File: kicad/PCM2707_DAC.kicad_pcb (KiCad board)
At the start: 2 copper layers, 49.5 x 38.1 mm, 37 parts, among them CON1 GND_CONNECTORSMD, J1 USB, Q1 12MHz, U1 PCM2707C

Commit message: Revert "Revert "Rounded corners on design, adding kicad generated gerbers""
This reverts commit e5d359f14d2e2aadcde64fe7d354a7193523fc92.
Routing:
- net /N$18: track 5.16 -> 3.01 mm
- net /N$17: track 5.04 -> 2.94 mm
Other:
- board size 49.5 x 38.1 mm -> 49.5 x 37.8 mm
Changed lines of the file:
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@@
     (links 79)
     (no_connects 0)
-    (area 148.704299 55.994299 198.259701 94.119701)
+    (area 147.0025 54.7497 198.20029 98.75012)
     (thickness 1.6)
     (drawings 6)
-    (tracks 211)
+    (tracks 209)
     (zones 0)
     (modules 37)
@@
     (40 Dwgs.User user)
     (41 Cmts.User user)
-    (42 Eco1.User user)
-    (43 Eco2.User user)
+    (42 Eco1.User user hide)
+    (43 Eco2.User user hide)
     (44 Edge.Cuts user)
   )
@@
     (pad_to_mask_clearance 0.2)
     (aux_axis_origin 0 0)
-    (visible_elements FFFFFFFF)
+    (visible_elements FFFDFFBF)
     (pcbplotparams
-      (layerselection 0x00030_80000001)
+      (layerselection 0x010ec_80000001)
       (usegerberextensions true)
       (excludeedgelayer true)
@@
       (outputformat 1)
       (mirror false)
-      (drillshape 1)
+      (drillshape 0)
       (scaleselection 1)
-      (outputdirectory ""))
+      (outputdirectory gerbers/))
   )
   (net 0 "")
@@
       (net 26 OL))
   )
-  (gr_line (start 198.247 56.007) (end 198.247 87.727) (layer Edge.Cuts) (width 0.0254))
-  (gr_line (start 198.247 87.727) (end 193.137 94.107) (layer Edge.Cuts) (width 0.0254))
-  (gr_line (start 193.137 94.107) (end 155.097 94.107) (layer Edge.Cuts) (width 0.0254))
-  (gr_line (start 155.097 94.107) (end 148.717 86.457) (layer Edge.Cuts) (width 0.0254))
-  (gr_line (start 148.717 86.457) (end 148.717 56.007) (layer Edge.Cuts) (width 0.0254))
-  (gr_line (start 148.717 56.007) (end 198.247 56.007) (layer Edge.Cuts) (width 0.0254))
+  (gr_line (start 198.12 56.134) (end 198.12 87.63) (angle 90) (layer Edge.Cuts) (width 0.15))
+  (gr_line (start 148.59 56.134) (end 198.12 56.134) (angle 90) (layer Edge.Cuts) (width 0.15))
+  (gr_line (start 148.59 86.868) (end 148.59 56.134) (angle 90) (layer Edge.Cuts) (width 0.15))
+  (gr_line (start 192.278 93.98) (end 155.702 93.98) (angle 90) (layer Edge.Cuts) (width 0.15))
+  (gr_arc (start 155.702 86.868) (end 155.702 93.98) (angle 90) (layer Edge.Cuts) (width 0.15))
+  (gr_arc (start 192.024 87.884) (end 198.12 87.63) (angle 90) (layer Edge.Cuts) (width 0.15))
   (segment (start 161.4424 70.555) (end 160.459 70.555) (width 0.4064) (layer Top) (net 1) (status 10))
   (segment (start 160.459 70.555) (end 159.119 69.215) (width 0.4064) (layer Top) (net 1) (status 20))
@@
   (segment (start 170.0276 72.955) (end 172.28 72.955) (width 0.4064) (layer Top) (net 8) (status 10))
   (segment (start 172.28 72.955) (end 172.72 73.395) (width 0.4064) (layer Top) (net 8) (status 20))
-  (segment (start 180.9115 70.11416) (end 178.1175 70.11416) (width 0.254) (layer Top) (net 9))
-  (segment (start 178.1175 70.11416) (end 178.06416 70.1675) (width 0.254) (layer Top) (net 9))
-  (segment (start 178.765 70.1675) (end 180.859 70.1675) (width 0.4064) (layer Top) (net 9) (status 30))
+  (segment (start 180.9115 70.11416) (end 178.1175 70.11416) (width 0.254) (layer Top) (net 9) (status 30))
+  (segment (start 178.1175 70.11416) (end 178.06416 70.1675) (width 0.254) (layer Top) (net 9) (status 30))
   (segment (start 180.859 70.1675) (end 180.9115 70.115) (width 0.4064) (layer Top) (net 9) (status 30))
-  (segment (start 178.06416 73.3425) (end 180.92166 73.3425) (width 0.254) (layer Top) (net 10))
-  (segment (start 180.92166 73.3425) (end 180.975 73.39584) (width 0.254) (layer Top) (net 10))
-  (segment (start 178.765 73.3425) (end 180.9225 73.3425) (width 0.4064) (layer Top) (net 10) (status 30))
+  (segment (start 178.06416 73.3425) (end 180.92166 73.3425) (width 0.254) (layer Top) (net 10) (status 30))
+  (segment (start 180.92166 73.3425) (end 180.975 73.39584) (width 0.254) (layer Top) (net 10) (status 30))
   (segment (start 180.9225 73.3425) (end 180.975 73.395) (width 0.4064) (layer Top) (net 10) (status 30))
   (segment (start 167.735 67.4624) (end 167.735 65.045) (width 0.4064) (layer Top) (net 11) (status 30))
   (segment (start 167.735 65.045) (end 168.01 64.77) (width 0.4064) (layer Top) (net 11) (status 30))
   (segment (start 170.0276 71.355) (end 174.3775 71.355) (width 0.4064) (layer Top) (net 12) (status 10))
-  (segment (start 174.3775 71.355) (end 175.565 70.1675) (width 0.4064) (layer Top) (net 12) (status 20))
-  (segment (start 175.565 70.1675) (end 176.2125 70.1675) (width 0.4064) (layer Top) (net 12) (status 10))
-  (segment (start 176.2125 70.1675) (end 177.8 68.58) (width 0.4064) (layer Top) (net 12))
+  (segment (start 174.3775 71.355) (end 175.565 70.1675) (width 0.4064) (layer Top) (net 12))
+  (segment (start 175.565 70.1675) (end 176.2125 70.1675) (width 0.4064) (layer Top) (net 12) (status 20))
+  (segment (start 176.2125 70.1675) (end 177.8 68.58) (width 0.4064) (layer Top) (net 12) (status 10))
   (segment (start 177.8 68.58) (end 179.07 68.58) (width 0.4064) (layer Top) (net 12))
   (segment (start 179.07 68.58) (end 179.705 67.945) (width 0.4064) (layer Top) (net 12))
@@
   (segment (start 157.365 69.215) (end 157.365 67.46) (width 0.4064) (layer Top) (net 13) (status 30))
   (segment (start 157.365 67.46) (end 157.215 67.31) (width 0.4064) (layer Top) (net 13) (status 30))
-  (segment (start 175.565 73.3425) (end 176.26584 73.3425) (width 0.254) (layer Top) (net 14))
+  (segment (start 175.565 73.3425) (end 176.26584 73.3425) (width 0.254) (layer Top) (net 14) (status 20))
   (segment (start 170.0276 72.155) (end 174.3775 72.155) (width 0.4064) (layer Top) (net 14) (status 10))
-  (segment (start 174.3775 72.155) (end 175.565 73.3425) (width 0.4064) (layer Top) (net 14) (status 20))
-  (segment (start 175.565 73.3425) (end 175.565 76.2) (width 0.4064) (layer Top) (net 14) (status 30))
+  (segment (start 174.3775 72.155) (end 175.565 73.3425) (width 0.4064) (layer Top) (net 14))
+  (segment (start 175.565 73.3425) (end 175.565 76.2) (width 0.4064) (layer Top) (net 14) (status 20))
   (segment (start 175.565 76.2) (end 175.565 78.194) (width 0.4064) (layer Top) (net 14) (status 30))
   (segment (start 175.565 78.194) (end 175.26 78.499) (width 0.4064) (layer Top) (net 14) (status 30))
@@
   (segment (start 167.005 81.165) (end 160.17 81.165) (width 0.4064) (layer Top) (net 23))
   (segment (start 160.17 81.165) (end 159.385 80.38) (width 0.4064) (layer Top) (net 23) (status 20))
-  (segment (start 168.91 90.805) (end 174.625 90.805) (width 0.254) (layer Bottom) (net 24))
+  (segment (start 168.91 90.805) (end 174.625 90.805) (width 0.254) (layer Bottom) (net 24) (status 10))
   (via (at 175.26 90.17) (size 0.889) (drill 0.635) (layers Top Bottom) (net 24))
-  (segment (start 175.26 90.17) (end 175.26 87.89416) (width 0.254) (layer Top) (net 24))
+  (segment (start 175.26 90.17) (end 175.26 87.89416) (width 0.254) (layer Top) (net 24) (status 20))
   (segment (start 174.625 90.805) (end 175.26 90.17) (width 0.254) (layer Bottom) (net 24))
   (via (at 172.72 76.835) (size 0.9048) (drill 0.6) (layers Top Bottom) (net 24))
@@
   (segment (start 189.495 60.0075) (end 189.495 58.155) (width 0.4064) (layer Top) (net 24) (status 10))
   (segment (start 189.495 58.155) (end 189.5475 58.1025) (width 0.4064) (layer Top) (net 24))
-  (segment (start 162.59 90.17) (end 162.59 88.87) (width 0.254) (layer Top) (net 25))
+  (segment (start 162.59 90.17) (end 162.59 88.87) (width 0.254) (layer Top) (net 25) (status 10))
   (via (at 163.83 87.63) (size 0.889) (drill 0.635) (layers Top Bottom) (net 25))
   (segment (start 162.59 88.87) (end 163.83 87.63) (width 0.254) (layer Top) (net 25))
-  (segment (start 167.005 90.805) (end 167.64 90.805) (width 0.254) (layer Bottom) (net 25))
+  (segment (start 167.005 90.805) (end 167.64 90.805) (width 0.254) (layer Bottom) (net 25) (status 30))
   (via (at 164.7825 78.105) (size 0.9048) (drill 0.6) (layers Top Bottom) (net 25))
   (via (at 166.0525 65.7225) (size 0.9048) (drill 0.6) (layers Top Bottom) (net 25))
@@
       (pts
         (xy 148.717 56.007) (xy 177.636494 55.980006) (xy 177.8 66.775006) (xy 172.72 66.675) (xy 167.64 70.485)
-        (xy 167.767 94.107) (xy 155.785991 94.107) (xy 148.717 88.392)
+        (xy 167.767 94.107) (xy 155.785991 94.107) (xy 151.384 92.456) (xy 148.717 88.392)
       )
     )
@@
     (polygon
       (pts
-        (xy 168.91 93.98) (xy 192.405 93.98) (xy 198.12 88.9) (xy 198.12 56.515) (xy 179.07 56.515)
-        (xy 179.07 67.945) (xy 173.355 67.945) (xy 168.91 71.12)
+        (xy 168.91 93.98) (xy 192.405 93.98) (xy 195.58 92.71) (xy 198.12 88.9) (xy 198.12 56.515)
+        (xy 179.07 56.515) (xy 179.07 67.945) (xy 173.355 67.945) (xy 168.91 71.12)
       )
     )

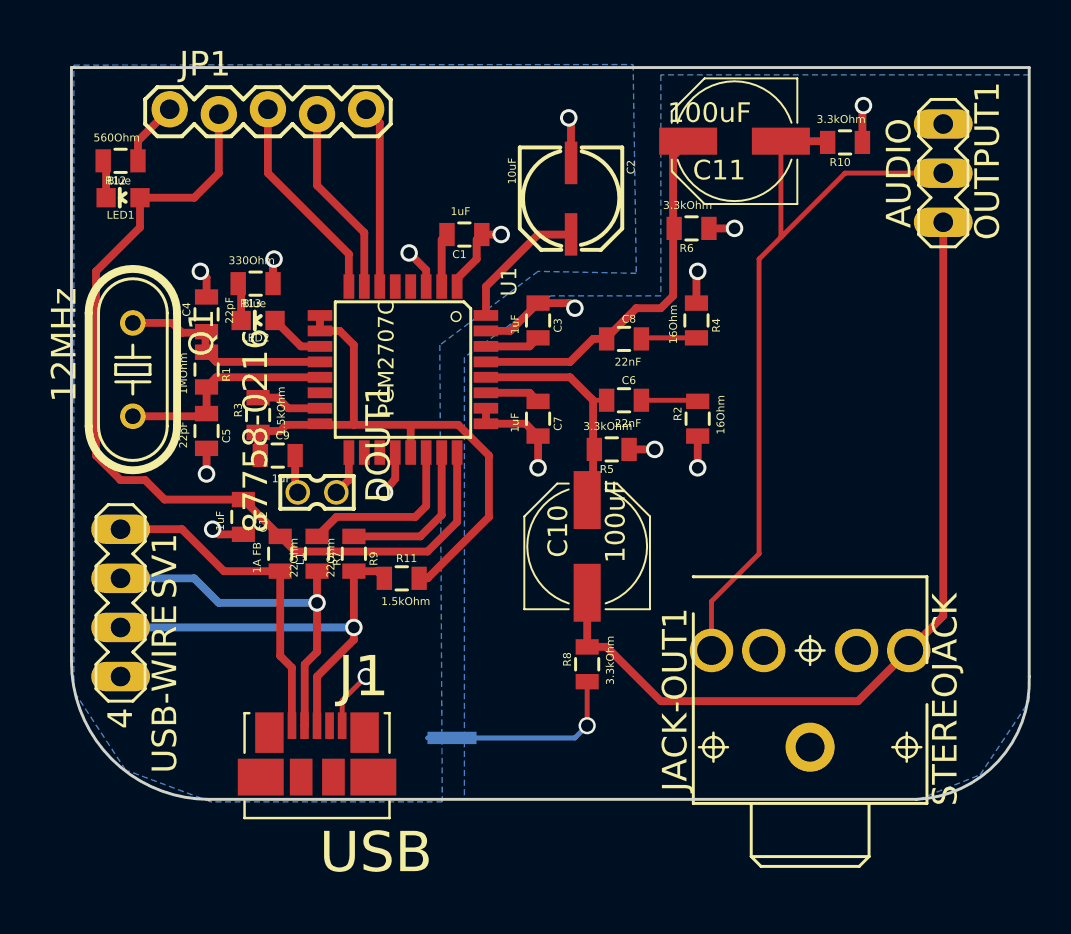
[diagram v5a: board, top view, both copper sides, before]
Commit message: Converted Libs
Converted PCM2707 libs from legacy to new version
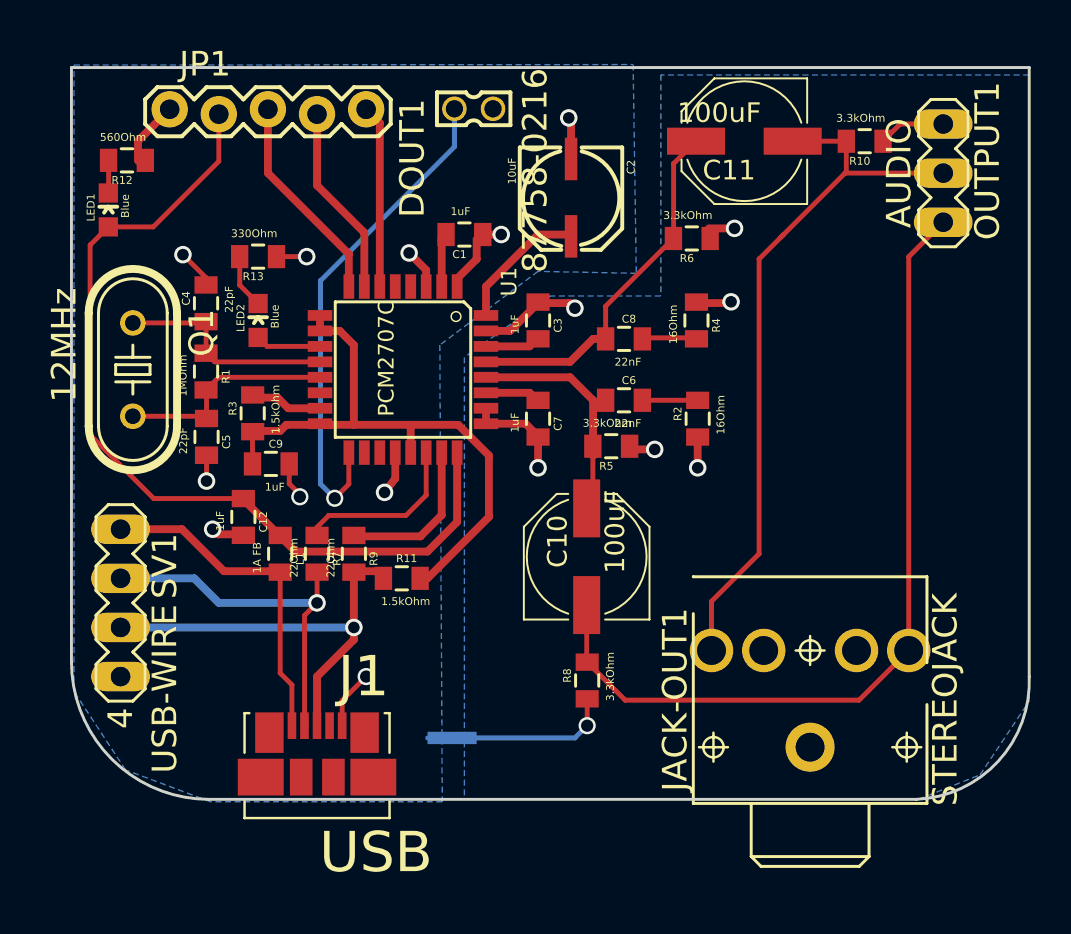
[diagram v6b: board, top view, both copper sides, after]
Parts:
- C1, C12, C3, C4, C5, C6, C7, C8, C9, L1, R1, R10, R11, R12, R13, R2, R3, R4, R5, R6, R7, R8, R9: footprint PCM2707_DAC:PASSIVES_0805 -> PCM2707:PASSIVES_0805
- C10, C11: footprint PCM2707_DAC:PASSIVES_PANASONIC_D -> PCM2707:PASSIVES_PANASONIC_D
- C2: footprint PCM2707_DAC:PASSIVES_PANASONIC_C -> PCM2707:PASSIVES_PANASONIC_C
- CON1: footprint PCM2707_DAC:GND_CONNECTOR -> PCM2707:GND_CONNECTOR
- DOUT1: footprint PCM2707_DAC:CON-MOLEX_87758-0216 -> PCM2707:CON-MOLEX_87758-0216
- J1: footprint PCM2707_DAC:MOLEX-47346-0001_MOLEX_47346-0001 -> PCM2707:MOLEX-47346-0001_MOLEX_47346-0001
- JACK-OUT1: footprint PCM2707_DAC:STX3100 -> PCM2707:STX3100
- JP1: footprint PCM2707_DAC:CONNECTORS_1X05_LOCK -> PCM2707:CONNECTORS_1X05_LOCK
- LED1, LED2: footprint PCM2707_DAC:LED_LED-0603 -> PCM2707:LED_LED-0603
- OUTPUT1: footprint PCM2707_DAC:CON-LSTB_MA03-1 -> PCM2707:CON-LSTB_MA03-1
- Q1: footprint PCM2707_DAC:CRYSTAL_HC49U-V -> PCM2707:CRYSTAL_HC49U-V
- SV1: footprint PCM2707_DAC:CON-LSTB_MA04-1 -> PCM2707:CON-LSTB_MA04-1
- U1: footprint PCM2707_DAC:PCM2707C -> PCM2707:PCM2707C
- moved DOUT1 21.4 mm to (169.4, 58.3), turned to 270 degrees
- moved R13 1.40 mm to (158.2, 65.9)
- moved R10 1.02 mm to (189.6, 59.9)
- moved LED1 0.99 mm to (150.5, 63.5), turned to 0 degrees
- moved R8 0.84 mm to (175.3, 87.8)
- moved C4 0.57 mm to (155.5, 68.3)
- moved C9 0.56 mm to (158.9, 76.6)
- moved C10 0.53 mm to (175.2, 81.4)
- moved R6 0.52 mm to (180.7, 65.0)
- moved C11 0.51 mm to (183.4, 59.9)
- moved R12 0.33 mm to (151.5, 60.9)
- moved C5 0.30 mm to (155.6, 75.2)
- moved R3 0.29 mm to (158.0, 74.0)
- moved R5 0.17 mm to (176.5, 75.7)
- moved R1 0.10 mm to (155.5, 71.9)
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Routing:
- net /N$6: track 2.32 -> 26.0 mm, vias 0 -> 1
- net OR: track 40.2 -> 37.3 mm
- net /N$23: track 12.4 -> 13.7 mm
- net /N$21: track 19.8 -> 18.8 mm
- net GND: track 25.7 -> 26.6 mm, vias 9 -> 10
- net /N$22: track 1.97 -> 2.82 mm
- net AGND: track 27.5 -> 28.3 mm, vias 8 -> 7
- net //SSPND: track 2.88 -> 3.39 mm
